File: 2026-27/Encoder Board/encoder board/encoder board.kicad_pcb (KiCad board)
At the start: 2 copper layers, 24 x 30 mm, 7 parts, among them J1 jst-ph, U1 TLE5012BE1000

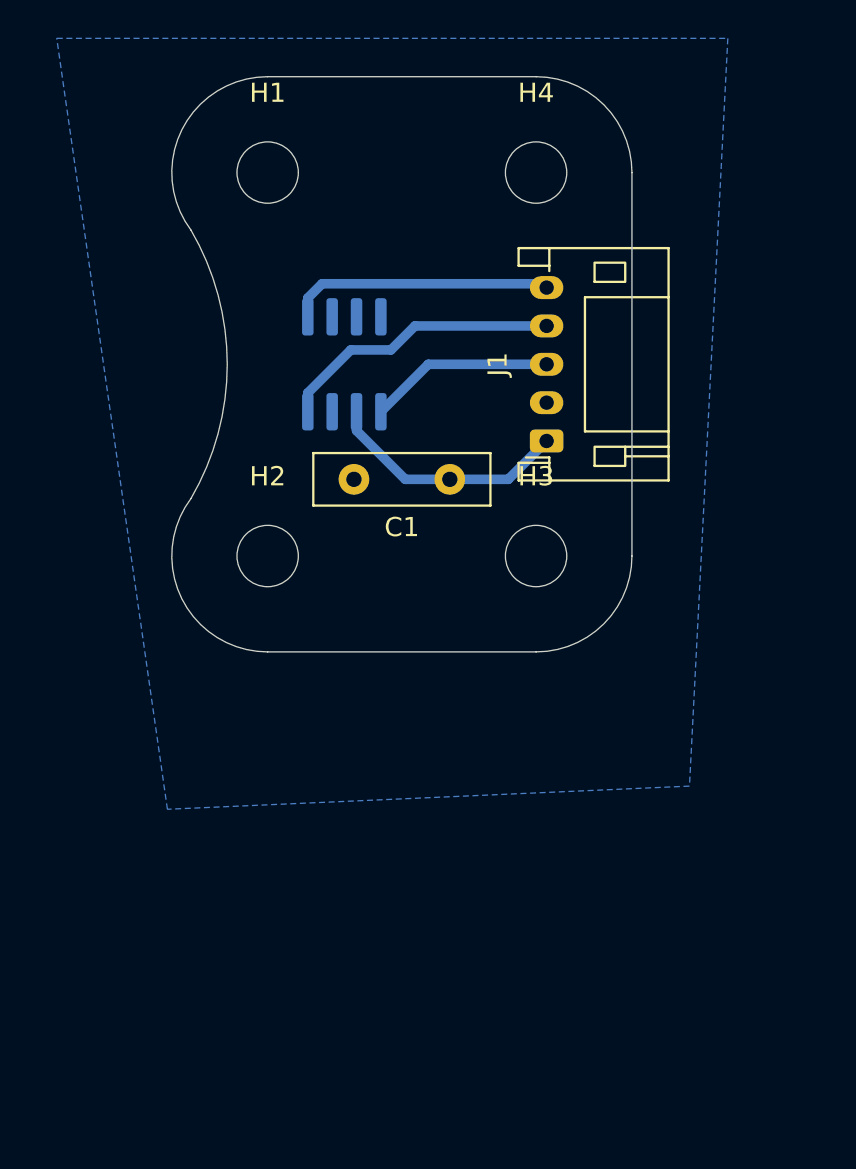
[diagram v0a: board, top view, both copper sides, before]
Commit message: encoder board
designed encoder board to mechanical team's size specifications
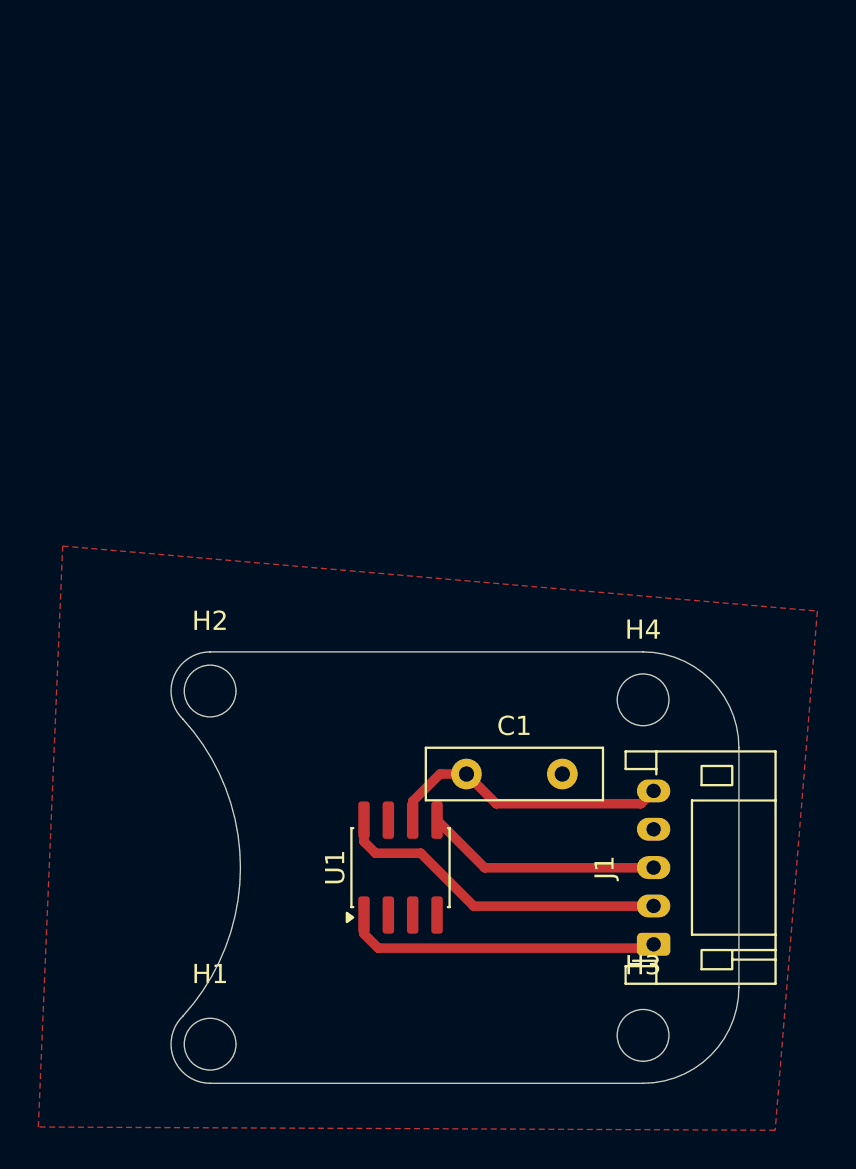
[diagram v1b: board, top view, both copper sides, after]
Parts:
- H1, H2, H3, H4: footprint MountingHole:MountingHole_3.2mm_M3 -> MountingHole:MountingHole_2.7mm_M2.5
- U1: moved to F.Cu
- moved H1 45.6 mm to (52.0, 100.5)
- moved H4 28.1 mm to (74.6, 82.5)
- moved J1 26.8 mm to (75.1, 95.2)
- moved U1 26.4 mm to (61.9, 91.2), turned to 90 degrees
- moved H3 25.6 mm to (74.6, 100.0)
- moved C1 15.4 mm to (65.4, 86.4), turned to 0 degrees
- moved H2 7.65 mm to (52.0, 82.0)
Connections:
- J1 pad 1: VDD -> /IFC
- J1 pad 2: GND -> VDD
- J1 pad 4: VDD -> GND
- J1 pad 5: /IFC -> VDD
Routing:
- net VDD: track 27.7 -> 32.7 mm
- net /IFA: track 9.67 -> 12.3 mm
- net /IFC: track 13.8 -> 16.5 mm
- added copper zone on F.Cu, net GND
- removed copper zone on B.Cu, net GND
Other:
- board size 24 x 30 mm -> 29.6 x 22.5 mm
